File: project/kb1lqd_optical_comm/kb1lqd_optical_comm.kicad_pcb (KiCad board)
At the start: 4 copper layers, 61 x 101.6 mm, 79 parts, among them J1 SJ1-3523N, J2 SJ-2509N, J3 SJ1-3523N, J4 Conn_01x04_Male, J5 Conn_01x02_Male, J6 SJ1-3523N, Q1 PMBF170, SW1 EG1213, SW2 EG1213, SW3 EG1213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

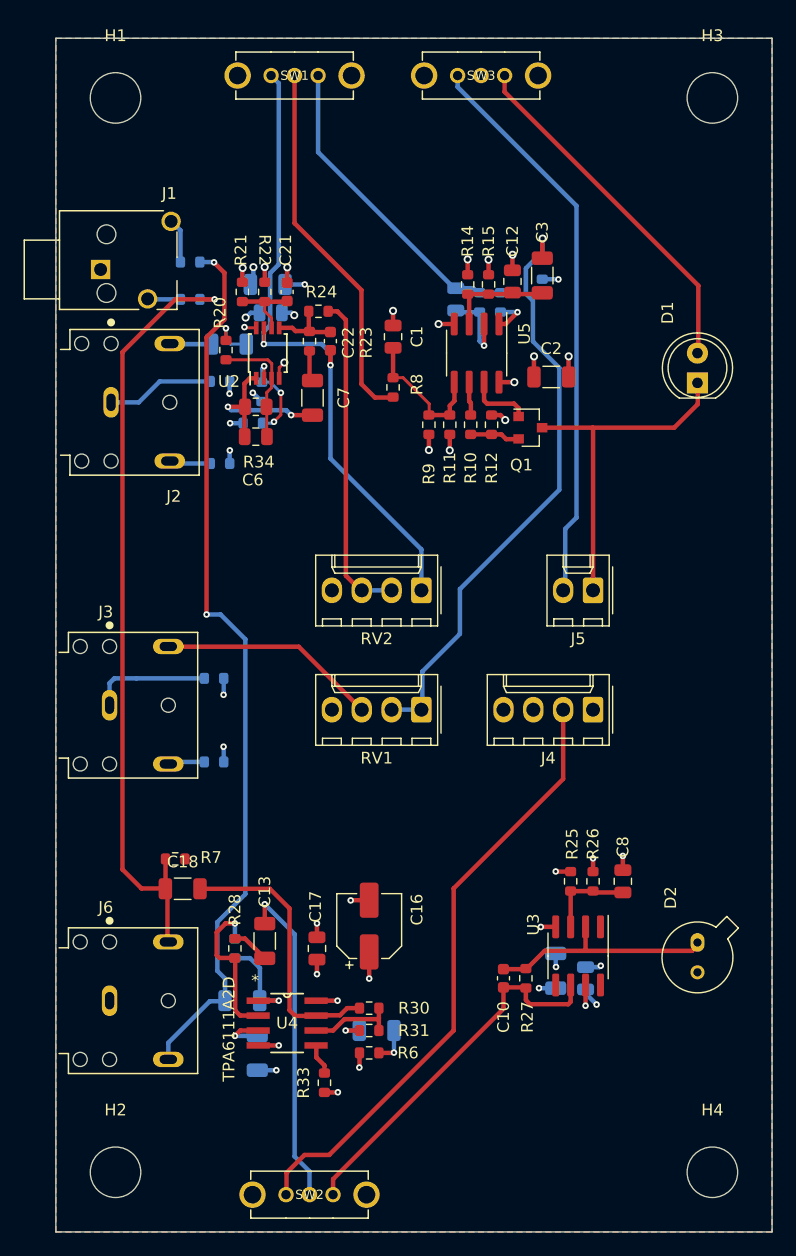
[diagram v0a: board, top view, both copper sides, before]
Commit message: Updated mounting holes. Created BOM.
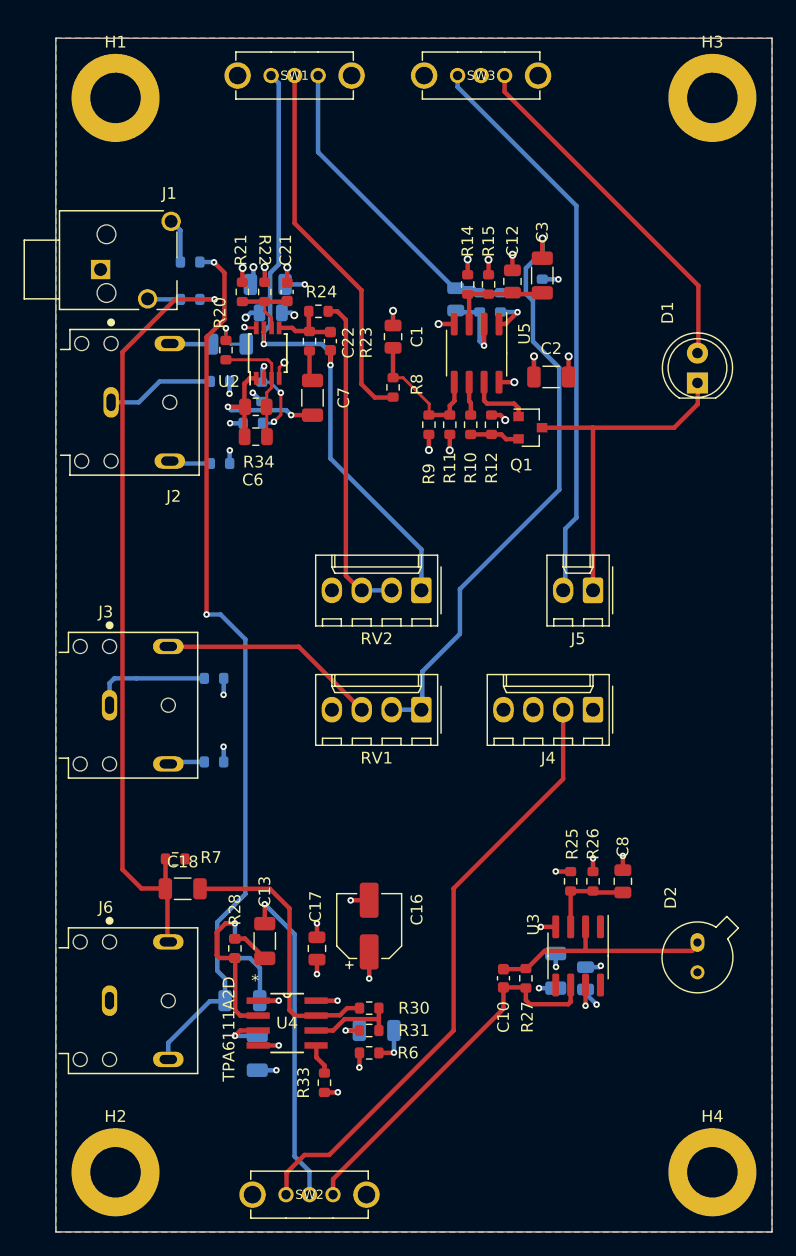
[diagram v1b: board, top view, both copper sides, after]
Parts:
- H1, H2, H3, H4: footprint MountingHole:MountingHole_4.3mm_M4 -> MountingHole:MountingHole_4.3mm_M4_DIN965_Pad
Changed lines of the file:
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@@
     (uvia_drill 0.1)
+  )
+  (module MountingHole:MountingHole_4.3mm_M4_DIN965_Pad (layer F.Cu)
+    (at 182.88 121.92)
+    (descr "Mounting Hole 4.3mm, M4, DIN965")
+    (tags "mounting hole 4.3mm m4 din965")
+    (attr virtual)
+    (fp_text reference H4 (at 0 -4.75) (layer F.SilkS)
+      (effects (font (size 1 1) (thickness 0.15)))
+    )
+    (fp_text value MountingHole_Pad (at 0 4.75) (layer F.Fab)
+      (effects (font (size 1 1) (thickness 0.15)))
+    )
+    (fp_text user %R (at 0.3 0) (layer F.Fab)
+      (effects (font (size 1 1) (thickness 0.15)))
+    )
+    (fp_circle (center 0 0) (end 3.75 0) (layer Cmts.User) (width 0.15))
+    (fp_circle (center 0 0) (end 4 0) (layer F.CrtYd) (width 0.05))
+    (pad 1 thru_hole circle (at 0 0) (size 7.5 7.5) (drill 4.3) (layers *.Cu *.Mask)
+      (net 1 GND))
+  )
+  (module MountingHole:MountingHole_4.3mm_M4_DIN965_Pad (layer F.Cu)
+    (at 182.88 30.48)
+    (descr "Mounting Hole 4.3mm, M4, DIN965")
+    (tags "mounting hole 4.3mm m4 din965")
+    (attr virtual)
+    (fp_text reference H3 (at 0 -4.75) (layer F.SilkS)
+      (effects (font (size 1 1) (thickness 0.15)))
+    )
+    (fp_text value MountingHole_Pad (at 0 4.75) (layer F.Fab)
+      (effects (font (size 1 1) (thickness 0.15)))
+    )
+    (fp_text user %R (at 0.3 0) (layer F.Fab)
+      (effects (font (size 1 1) (thickness 0.15)))
+    )
+    (fp_circle (center 0 0) (end 3.75 0) (layer Cmts.User) (width 0.15))
+    (fp_circle (center 0 0) (end 4 0) (layer F.CrtYd) (width 0.05))
+    (pad 1 thru_hole circle (at 0 0) (size 7.5 7.5) (drill 4.3) (layers *.Cu *.Mask)
+      (net 1 GND))
+  )
+  (module MountingHole:MountingHole_4.3mm_M4_DIN965_Pad (layer F.Cu)
+    (at 132.08 121.92)
+    (descr "Mounting Hole 4.3mm, M4, DIN965")
+    (tags "mounting hole 4.3mm m4 din965")
+    (attr virtual)
+    (fp_text reference H2 (at 0 -4.75) (layer F.SilkS)
+      (effects (font (size 1 1) (thickness 0.15)))
+    )
+    (fp_text value MountingHole_Pad (at 0 4.75) (layer F.Fab)
+      (effects (font (size 1 1) (thickness 0.15)))
+    )
+    (fp_text user %R (at 0.3 0) (layer F.Fab)
+      (effects (font (size 1 1) (thickness 0.15)))
+    )
+    (fp_circle (center 0 0) (end 3.75 0) (layer Cmts.User) (width 0.15))
+    (fp_circle (center 0 0) (end 4 0) (layer F.CrtYd) (width 0.05))
+    (pad 1 thru_hole circle (at 0 0) (size 7.5 7.5) (drill 4.3) (layers *.Cu *.Mask)
+      (net 1 GND))
+  )
+  (module MountingHole:MountingHole_4.3mm_M4_DIN965_Pad (layer F.Cu)
+    (at 132.08 30.48)
+    (descr "Mounting Hole 4.3mm, M4, DIN965")
+    (tags "mounting hole 4.3mm m4 din965")
+    (attr virtual)
+    (fp_text reference H1 (at 0 -4.75) (layer F.SilkS)
+      (effects (font (size 1 1) (thickness 0.15)))
+    )
+    (fp_text value MountingHole_Pad (at 0 4.75) (layer F.Fab)
+      (effects (font (size 1 1) (thickness 0.15)))
+    )
+    (fp_text user %R (at 0.3 0) (layer F.Fab)
+      (effects (font (size 1 1) (thickness 0.15)))
+    )
+    (fp_circle (center 0 0) (end 3.75 0) (layer Cmts.User) (width 0.15))
+    (fp_circle (center 0 0) (end 4 0) (layer F.CrtYd) (width 0.05))
+    (pad 1 thru_hole circle (at 0 0) (size 7.5 7.5) (drill 4.3) (layers *.Cu *.Mask)
+      (net 1 GND))
   )
   (module SJ1-3523N:CUI_SJ1-3523N (layer F.Cu)
@@
       (net 31 "Net-(J1-Pad1)"))
   )
-  (module MountingHole:MountingHole_4.3mm_M4 (layer F.Cu)
-    (at 132.08 30.48)
-    (descr "Mounting Hole 4.3mm, no annular, M4")
-    (tags "mounting hole 4.3mm no annular m4")
-    (attr virtual)
-    (fp_text reference H1 (at 0 -5.3) (layer F.SilkS)
-      (effects (font (size 1 1) (thickness 0.15)))
-    )
-    (fp_text value MountingHole_Pad (at 0 5.3) (layer F.Fab)
-      (effects (font (size 1 1) (thickness 0.15)))
-    )
-    (fp_circle (center 0 0) (end 4.55 0) (layer F.CrtYd) (width 0.05))
-    (fp_circle (center 0 0) (end 4.3 0) (layer Cmts.User) (width 0.15))
-    (fp_text user %R (at 0.3 0) (layer F.Fab)
-      (effects (font (size 1 1) (thickness 0.15)))
-    )
-    (pad 1 np_thru_hole circle (at 0 0) (size 4.3 4.3) (drill 4.3) (layers *.Cu *.Mask)
-      (net 1 GND))
-  )
-  (module MountingHole:MountingHole_4.3mm_M4 (layer F.Cu)
-    (at 182.88 121.92)
-    (descr "Mounting Hole 4.3mm, no annular, M4")
-    (tags "mounting hole 4.3mm no annular m4")
-    (attr virtual)
-    (fp_text reference H4 (at 0 -5.3) (layer F.SilkS)
-      (effects (font (size 1 1) (thickness 0.15)))
-    )
-    (fp_text value MountingHole_Pad (at 0 5.3) (layer F.Fab)
-      (effects (font (size 1 1) (thickness 0.15)))
-    )
-    (fp_circle (center 0 0) (end 4.55 0) (layer F.CrtYd) (width 0.05))
-    (fp_circle (center 0 0) (end 4.3 0) (layer Cmts.User) (width 0.15))
-    (fp_text user %R (at 0.3 0) (layer F.Fab)
-      (effects (font (size 1 1) (thickness 0.15)))
-    )
-    (pad 1 np_thru_hole circle (at 0 0) (size 4.3 4.3) (drill 4.3) (layers *.Cu *.Mask)
-      (net 1 GND))
-  )
-  (module MountingHole:MountingHole_4.3mm_M4 (layer F.Cu)
-    (at 182.88 30.48)
-    (descr "Mounting Hole 4.3mm, no annular, M4")
-    (tags "mounting hole 4.3mm no annular m4")
-    (attr virtual)
-    (fp_text reference H3 (at 0 -5.3) (layer F.SilkS)
-      (effects (font (size 1 1) (thickness 0.15)))
-    )
-    (fp_text value MountingHole_Pad (at 0 5.3) (layer F.Fab)
-      (effects (font (size 1 1) (thickness 0.15)))
-    )
-    (fp_circle (center 0 0) (end 4.55 0) (layer F.CrtYd) (width 0.05))
-    (fp_circle (center 0 0) (end 4.3 0) (layer Cmts.User) (width 0.15))
-    (fp_text user %R (at 0.3 0) (layer F.Fab)
-      (effects (font (size 1 1) (thickness 0.15)))
-    )
-    (pad 1 np_thru_hole circle (at 0 0) (size 4.3 4.3) (drill 4.3) (layers *.Cu *.Mask)
-      (net 1 GND))
-  )
-  (module MountingHole:MountingHole_4.3mm_M4 (layer F.Cu)
-    (at 132.08 121.92)
-    (descr "Mounting Hole 4.3mm, no annular, M4")
-    (tags "mounting hole 4.3mm no annular m4")
-    (attr virtual)
-    (fp_text reference H2 (at 0 -5.3) (layer F.SilkS)
-      (effects (font (size 1 1) (thickness 0.15)))
-    )
-    (fp_text value MountingHole_Pad (at 0 5.3) (layer F.Fab)
-      (effects (font (size 1 1) (thickness 0.15)))
-    )
-    (fp_circle (center 0 0) (end 4.55 0) (layer F.CrtYd) (width 0.05))
-    (fp_circle (center 0 0) (end 4.3 0) (layer Cmts.User) (width 0.15))
-    (fp_text user %R (at 0.3 0) (layer F.Fab)
-      (effects (font (size 1 1) (thickness 0.15)))
-    )
-    (pad 1 np_thru_hole circle (at 0 0) (size 4.3 4.3) (drill 4.3) (layers *.Cu *.Mask)
-      (net 1 GND))
-  )
   (module EG1213:SW_EG1213 (layer F.Cu)

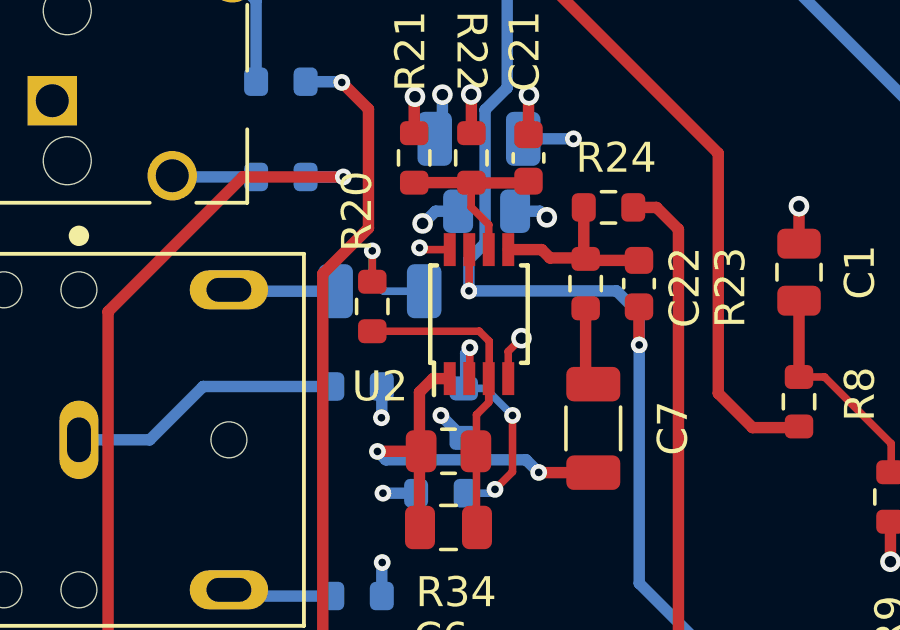
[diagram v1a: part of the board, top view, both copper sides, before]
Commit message: Updated u2 to soic 8
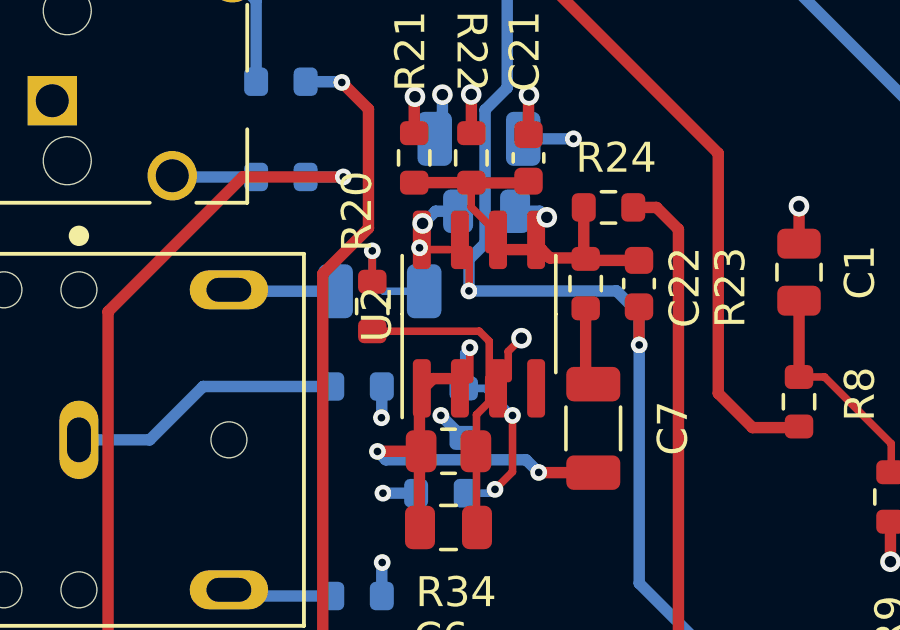
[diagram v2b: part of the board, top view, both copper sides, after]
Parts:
- U2: footprint Package_SO:TSSOP-8_3x3mm_P0.65mm -> Package_SO:SOIC-8_3.9x4.9mm_P1.27mm

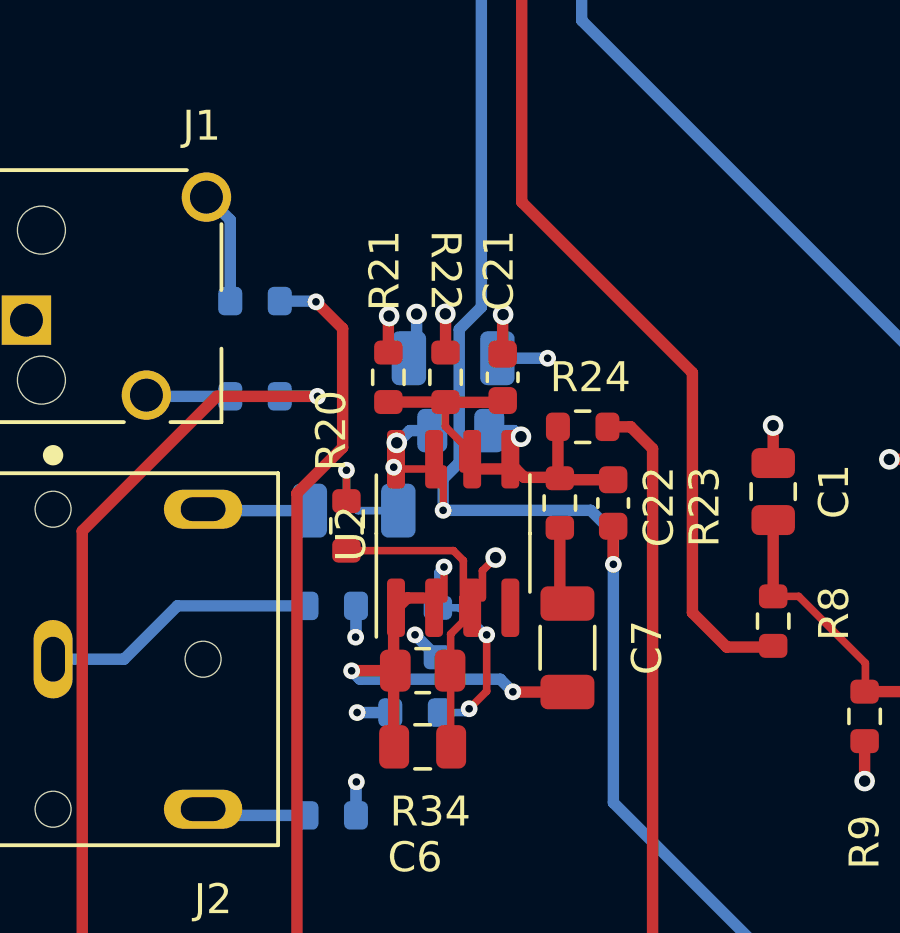
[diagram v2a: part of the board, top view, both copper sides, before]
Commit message: Updated to new soic footprint.
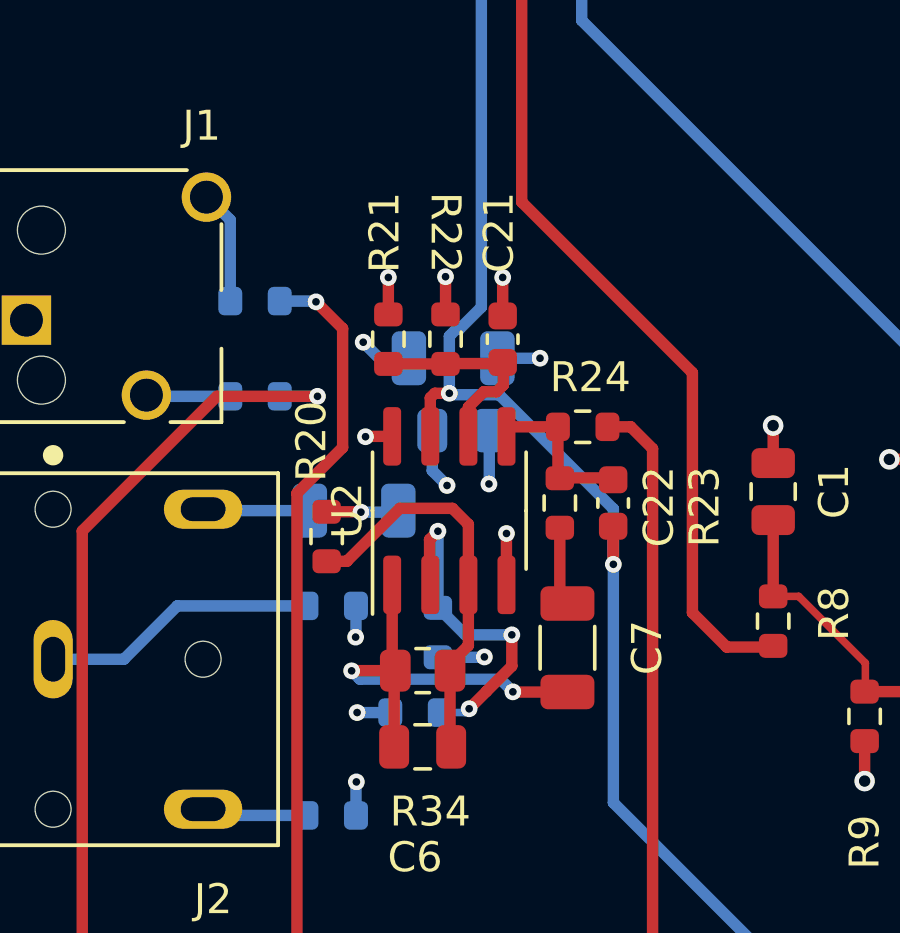
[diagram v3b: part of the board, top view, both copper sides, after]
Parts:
- moved C21 1.27 mm to (146.7, 45.7)
- moved R21 1.27 mm to (142.9, 45.7)
- moved R22 1.27 mm to (144.8, 45.7)
- moved U2 0.77 mm to (144.9, 51.4)
- moved R20 0.75 mm to (140.8, 52.3)
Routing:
- net Net-(R18-Pad1): track 8.45 -> 11.4 mm
- net Net-(C6-Pad2): track 10.5 -> 13.3 mm
- net GND: track 37.6 -> 39.1 mm
- net Net-(C5-Pad1): track 3.87 -> 2.50 mm
- net Net-(C22-Pad2): track 6.22 -> 5.27 mm
- net Net-(C21-Pad1): track 6.39 -> 7.03 mm

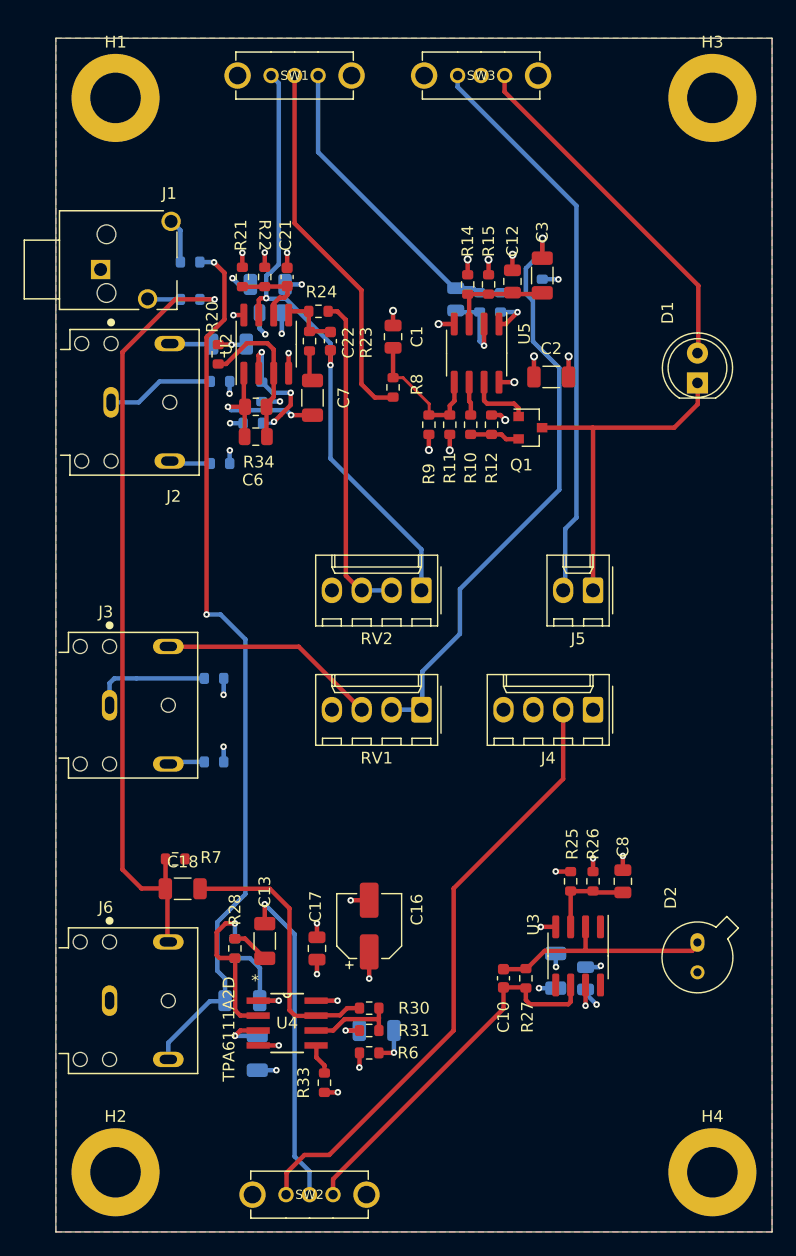
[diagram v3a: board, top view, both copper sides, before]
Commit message: Fixed a few errors in silkscreen, found an open item error in U3 generated footprint.
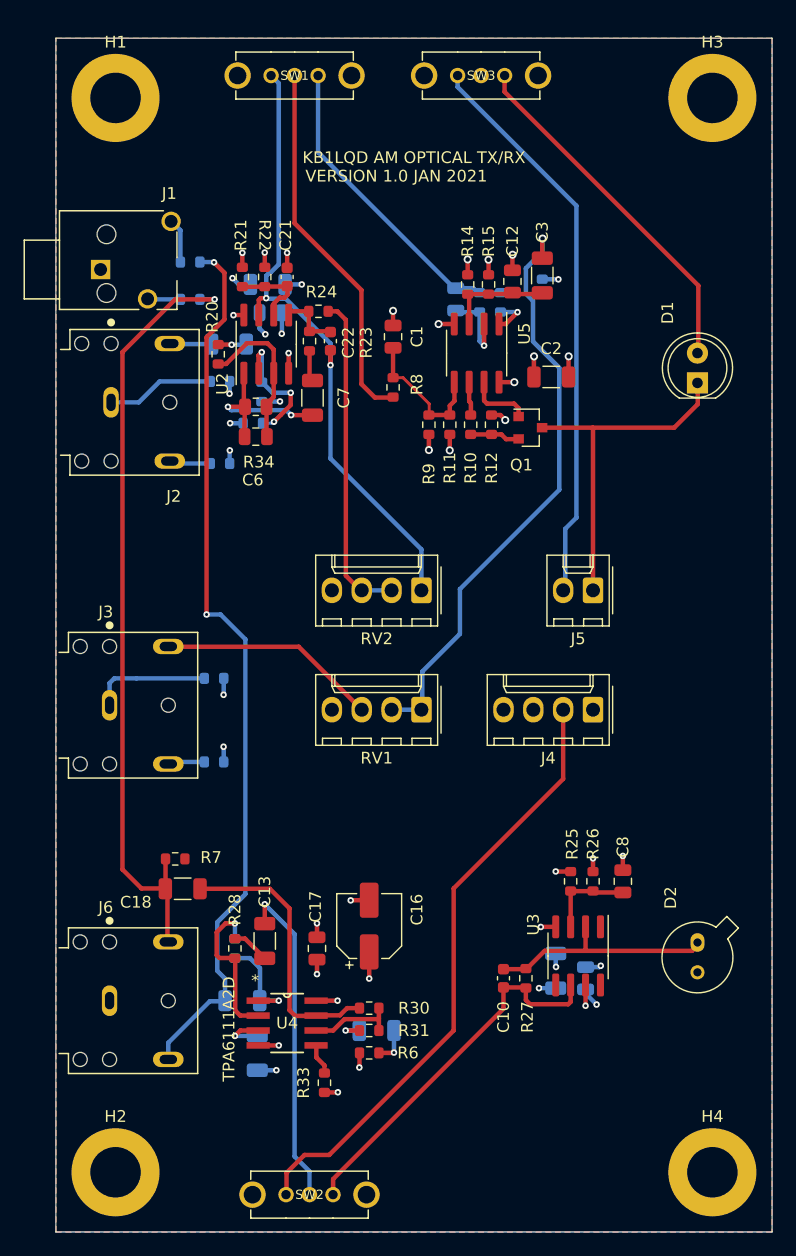
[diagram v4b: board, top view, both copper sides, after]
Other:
- board text added: "KB1LQD AM OPTICAL TX/RX"
- board text added: "VERSION 1.0 JAN 2021"
